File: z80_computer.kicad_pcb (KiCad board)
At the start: 4 copper layers, 21 parts, among them J1 Screw_Terminal_01x02, J2 Bus_ISA_8bit, U1 74LS14, U2 MCP130, U3 LM117_TO3, U4 74LS32, U5 Z80CPU, Y1 Crystal

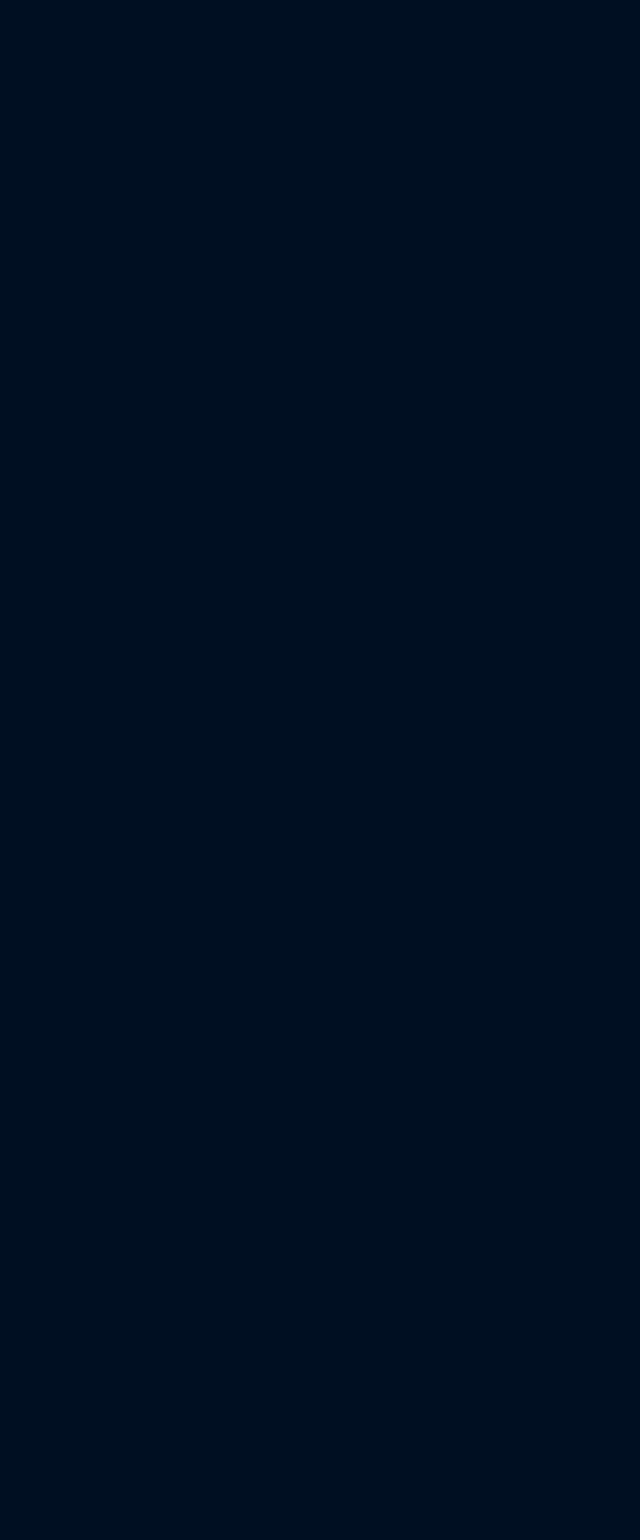
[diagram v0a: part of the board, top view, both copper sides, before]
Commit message: Added ISA bus, broke some circuits into sub schematics.
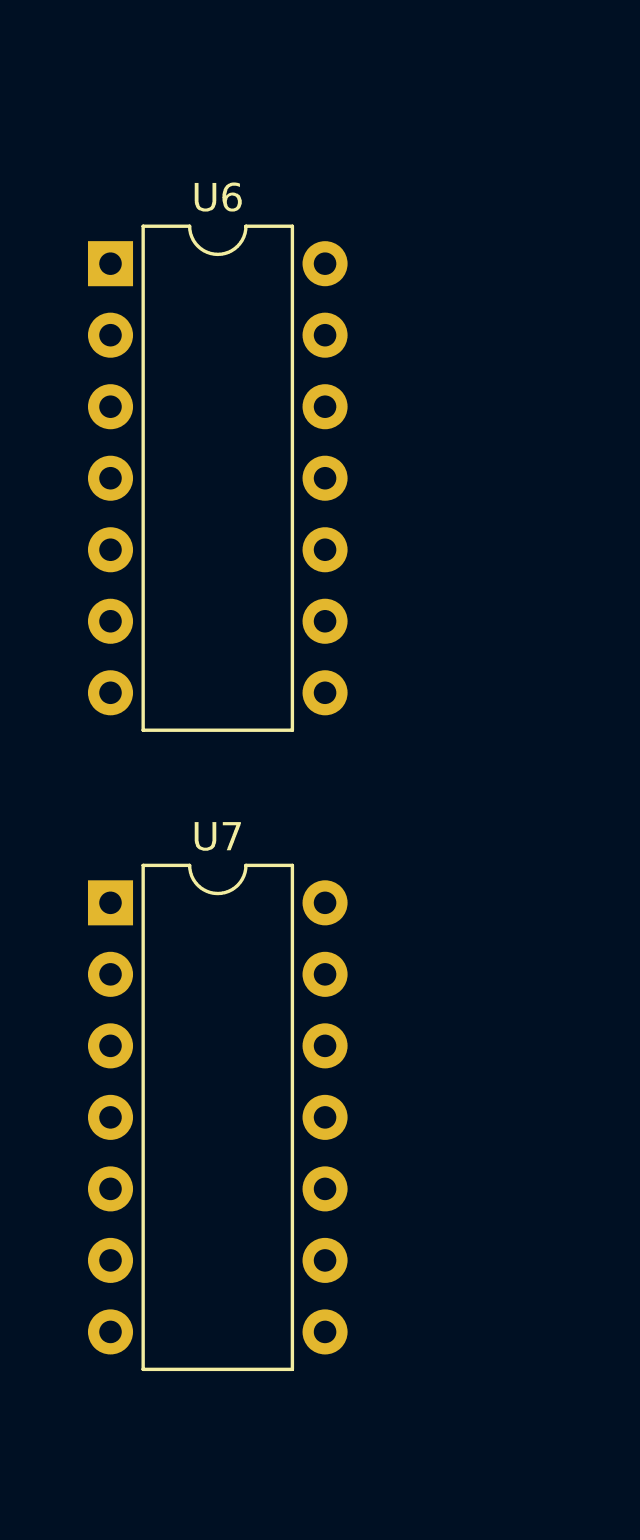
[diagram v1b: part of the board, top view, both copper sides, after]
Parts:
- added U6: 74LS32, Package_DIP:DIP-14_W7.62mm, F.Cu at (30.3, 86.7)
- added U7: 74LS73, Package_DIP:DIP-14_W7.62mm, F.Cu at (30.3, 109.4)
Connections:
- J2 pad 10: Net-(J2-Pad10) -> GND
- J2 pad 11: Net-(J2-Pad11) -> /~MEMWR
- J2 pad 12: Net-(J2-Pad12) -> /~MEMRD
- J2 pad 13: Net-(J2-Pad13) -> /~IOWR
- J2 pad 14: Net-(J2-Pad14) -> /~IORD
- J2 pad 2: Net-(J2-Pad2) -> /~RST
- J2 pad 20: Net-(J2-Pad20) -> /~CLK
- J2 pad 29: Net-(J2-Pad29) -> +5V

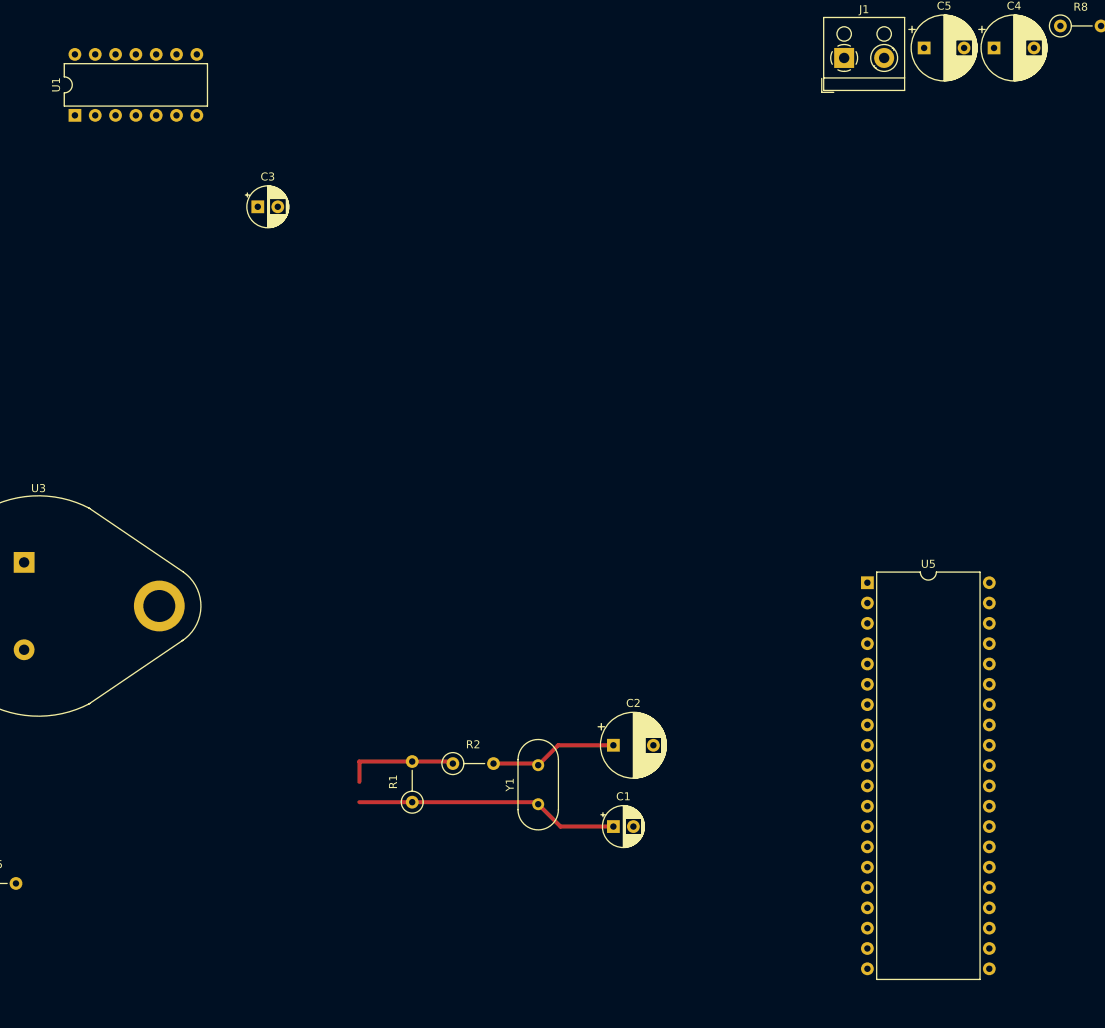
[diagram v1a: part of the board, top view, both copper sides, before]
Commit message: Added some temporary footprints and messed with the oscillator layout
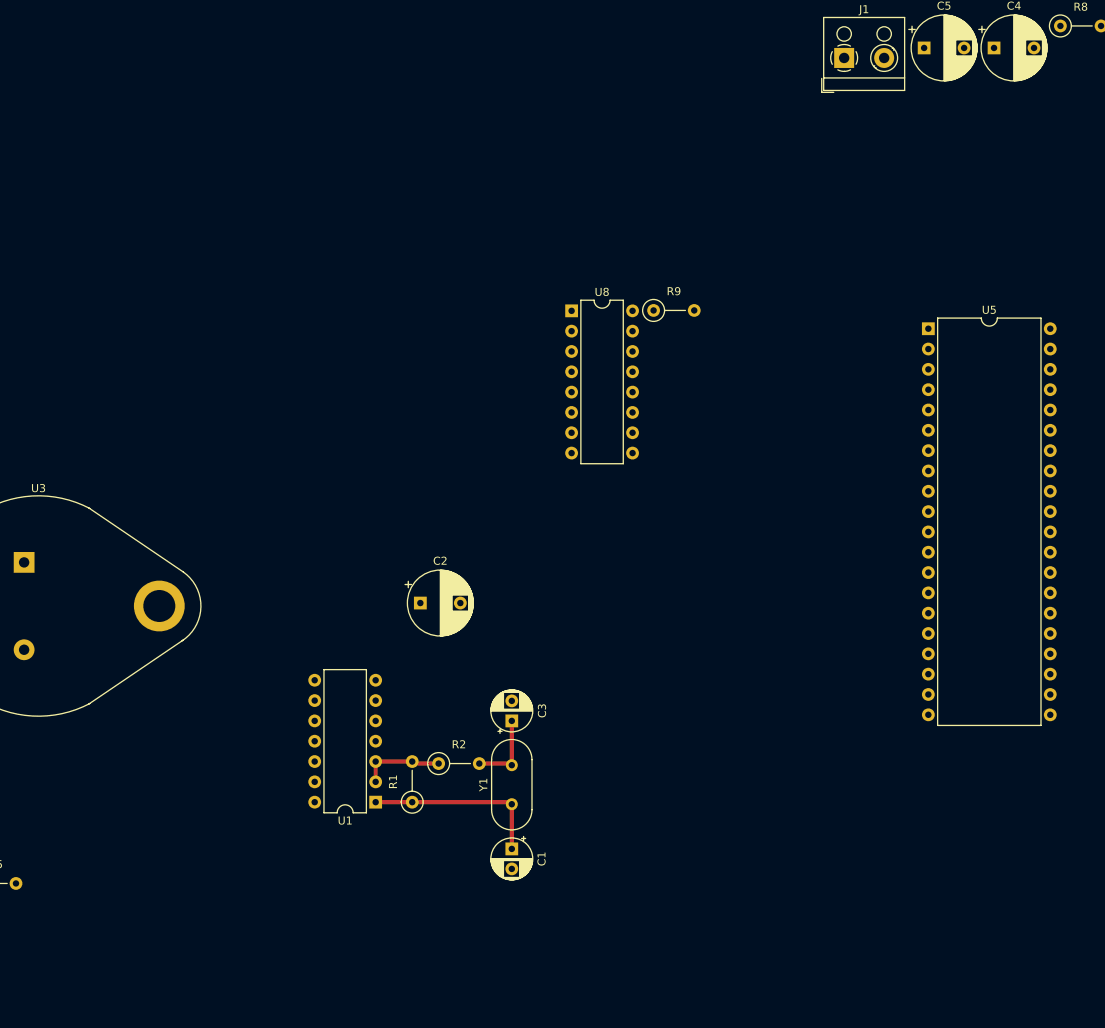
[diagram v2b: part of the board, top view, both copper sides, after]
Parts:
- added R9: 10K, Resistor_THT:R_Axial_DIN0207_L6.3mm_D2.5mm_P5.08mm_Vertical, F.Cu at (152.3, 75.2)
- added U8: 74138, Package_DIP:DIP-16_W7.62mm, F.Cu at (142.1, 75.2)
- moved U1 93.7 mm to (117.6, 136.7), turned to 180 degrees
- moved C3 71.7 mm to (134.6, 126.5), turned to 90 degrees
- moved U5 32.7 mm to (186.7, 77.5)
- moved C2 30.0 mm to (123.2, 111.8)
- moved C1 13.0 mm to (134.6, 142.5), turned to 270 degrees
- moved Y1 3.30 mm to (134.6, 136.9)
- moved R2 1.78 mm to (125.5, 131.8)
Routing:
- net GND: track 0.00 -> 17.8 mm
- net Net-(C2-Pad1): track 16.1 -> 0.00 mm
- net Net-(C1-Pad1): track 33.0 -> 22.7 mm
- net Net-(C3-Pad1): track 0.00 -> 9.68 mm
- net Net-(R1-Pad2): track 14.3 -> 10.9 mm
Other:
- net class Default: clearance 0.2 -> 0.1524; trace_width 0.25 -> 0.254; via_dia 0.8 -> 0.8128; via_drill 0.4 -> 0.4318
- rule trace_clearance: 0.2 -> 0.1524
